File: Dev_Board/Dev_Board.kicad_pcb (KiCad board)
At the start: 2 copper layers, 41 x 67.7 mm, 31 parts, among them J1 Conn_01x04, J2 Conn_01x04

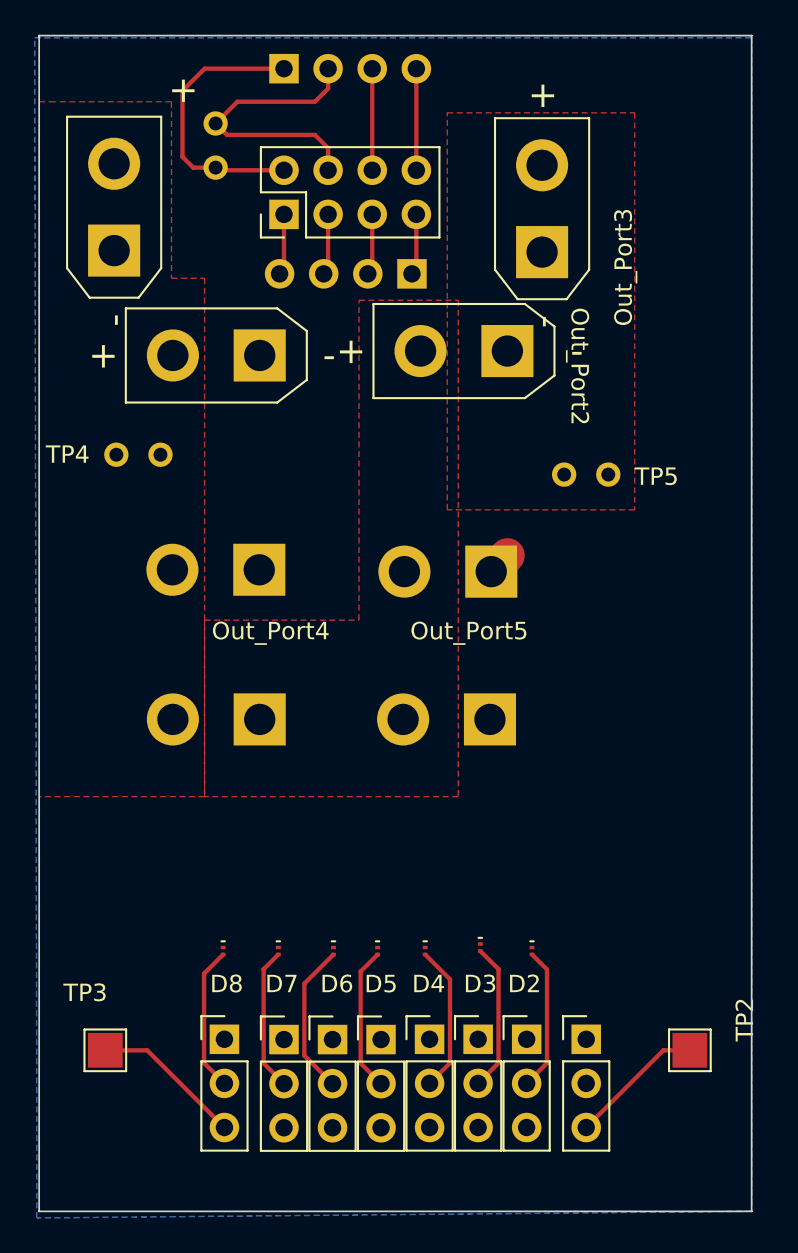
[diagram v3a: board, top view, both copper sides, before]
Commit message: Changed location of connectors of I2C and added mounting holes. Also I'm currently adding pads for the diodes
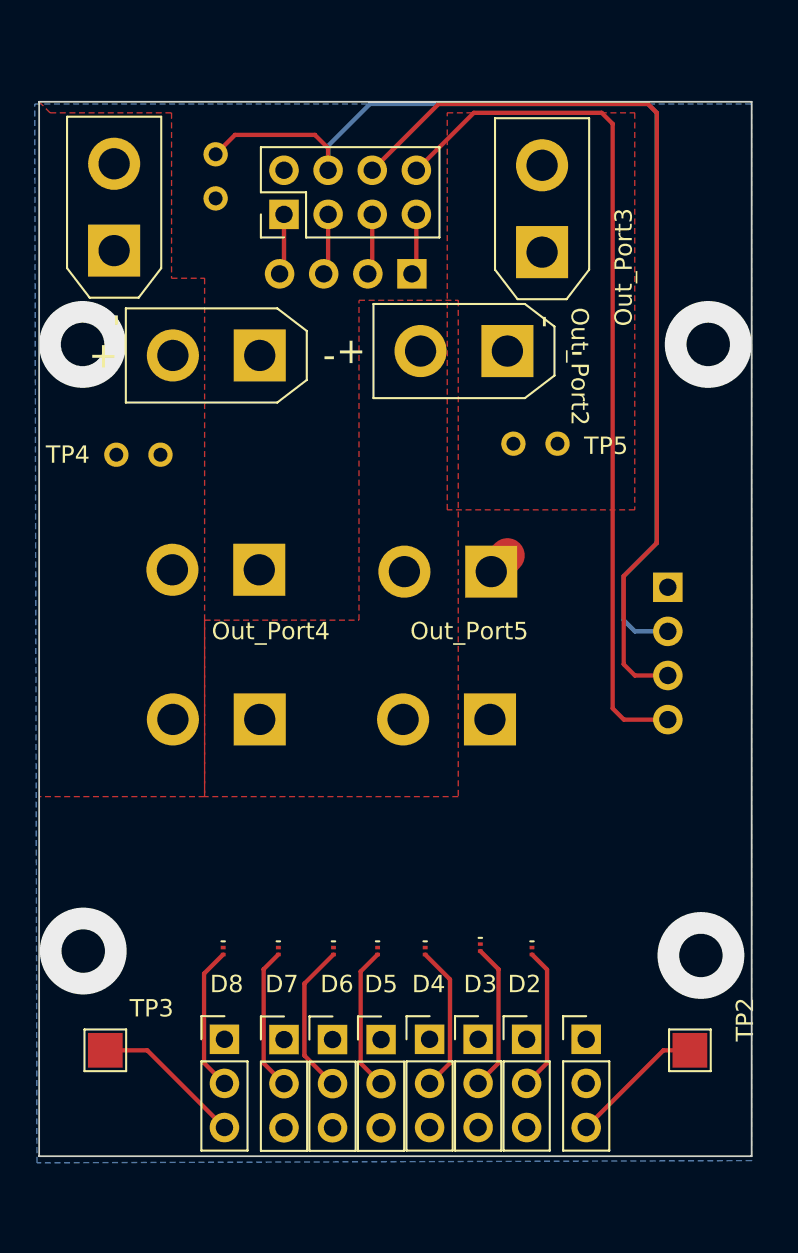
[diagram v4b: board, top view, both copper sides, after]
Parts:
- moved J2 37.1 mm to (222.2, 61.6), turned to 180 degrees
- moved TP5 3.42 mm to (213.4, 53.3)
- moved TP1 1.77 mm to (196.2, 39.2)
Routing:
- net /I2C2_SCL: track 5.85 -> 53.5 mm
- net +3.3V: track 16.8 -> 62.9 mm
- net /I2C2_SDA: track 5.85 -> 50.0 mm
- net GND: track 19.2 -> 3.06 mm, vias 0 -> 4
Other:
- board size 41 x 67.7 mm -> 41 x 60.7 mm

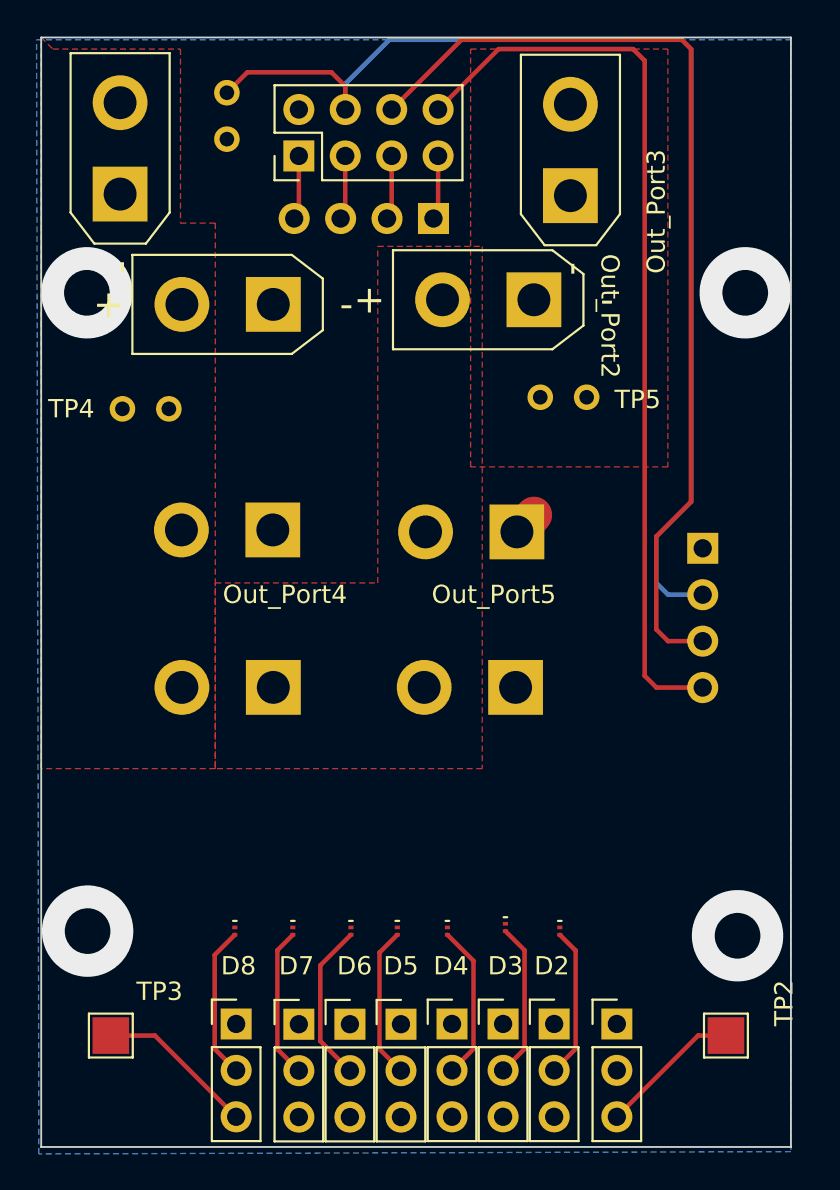
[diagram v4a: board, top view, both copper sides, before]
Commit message: fixed more sizing issues and I added a 1x4 connector to the data pins
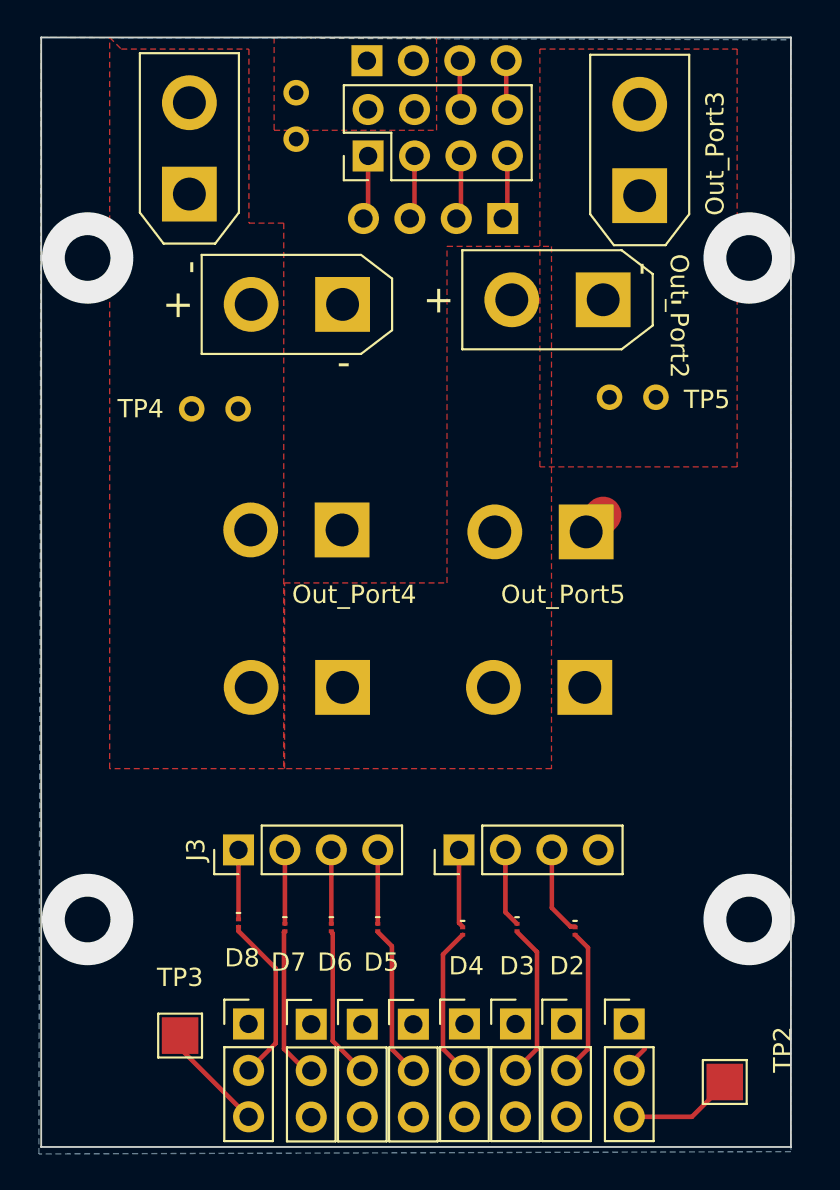
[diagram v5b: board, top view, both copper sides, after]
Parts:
- added J3: Conn_01x04, Connector_PinHeader_2.54mm:PinHeader_1x04_P2.54mm_Vertical, F.Cu at (196.8, 78.1)
- added J4: Conn_01x04, Connector_PinHeader_2.54mm:PinHeader_1x04_P2.54mm_Vertical, F.Cu at (208.9, 78.1)
- moved J2 32.4 mm to (203.9, 34.9), turned to -90 degrees
- moved IO_Port1 3.79 mm to (203.9, 40.1)
- moved In_Port1 3.79 mm to (194.2, 42.1)
- moved Out_Port4 3.79 mm to (202.4, 60.6)
- moved TP4 3.79 mm to (196.8, 54.0)
- moved In_Port2 3.79 mm to (202.4, 69.2)
- moved J1 3.79 mm to (211.3, 43.6)
- moved Out_Port1 3.79 mm to (202.4, 48.3)
- moved Out_Port2 3.79 mm to (216.7, 48.0)
- moved Out_Port3 3.79 mm to (218.8, 42.2)
- moved Out_Port5 3.79 mm to (215.8, 60.7)
- moved Out_Port6 3.79 mm to (215.7, 69.2)
- moved TP1 3.79 mm to (200.0, 39.2)
- moved TP3 3.79 mm to (193.7, 88.3)
- moved TP5 3.79 mm to (217.2, 53.3)
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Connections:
- D2 pad 1: unconnected-(D2-K-Pad1) -> Net-(D2-K)
- D3 pad 1: unconnected-(D3-K-Pad1) -> Net-(D3-K)
- D4 pad 1: unconnected-(D4-K-Pad1) -> Net-(D4-K)
- D5 pad 1: unconnected-(D5-K-Pad1) -> Net-(D5-K)
- D6 pad 1: unconnected-(D6-K-Pad1) -> Net-(D6-K)
- D7 pad 1: unconnected-(D7-K-Pad1) -> Net-(D7-K)
- D8 pad 1: unconnected-(D8-K-Pad1) -> Net-(D8-K)
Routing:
- net +3.3V: track 62.9 -> 0.00 mm
- net /I2C2_SCL: track 53.5 -> 2.70 mm
- net /I2C2_SDA: track 50.0 -> 2.70 mm
- net Net-(D2-K): track 0.00 -> 4.87 mm
- net Net-(D3-K): track 0.00 -> 4.31 mm
- net Net-(D4-K): track 0.00 -> 4.28 mm
- net Net-(D7-K): track 0.00 -> 4.05 mm
- net Net-(D6-K): track 0.00 -> 4.05 mm
- net Net-(D5-K): track 0.00 -> 4.05 mm
- net Net-(D8-K): track 0.00 -> 3.76 mm
- net /C8: track 8.70 -> 6.00 mm
- net /C1: track 7.81 -> 6.12 mm
- net /B1 (5V): track 0.00 -> 1.66 mm
- net /B8 (5V): track 8.36 -> 9.31 mm
- net /B6: track 8.80 -> 8.29 mm
- added copper zone on F.Cu, net +3.3V

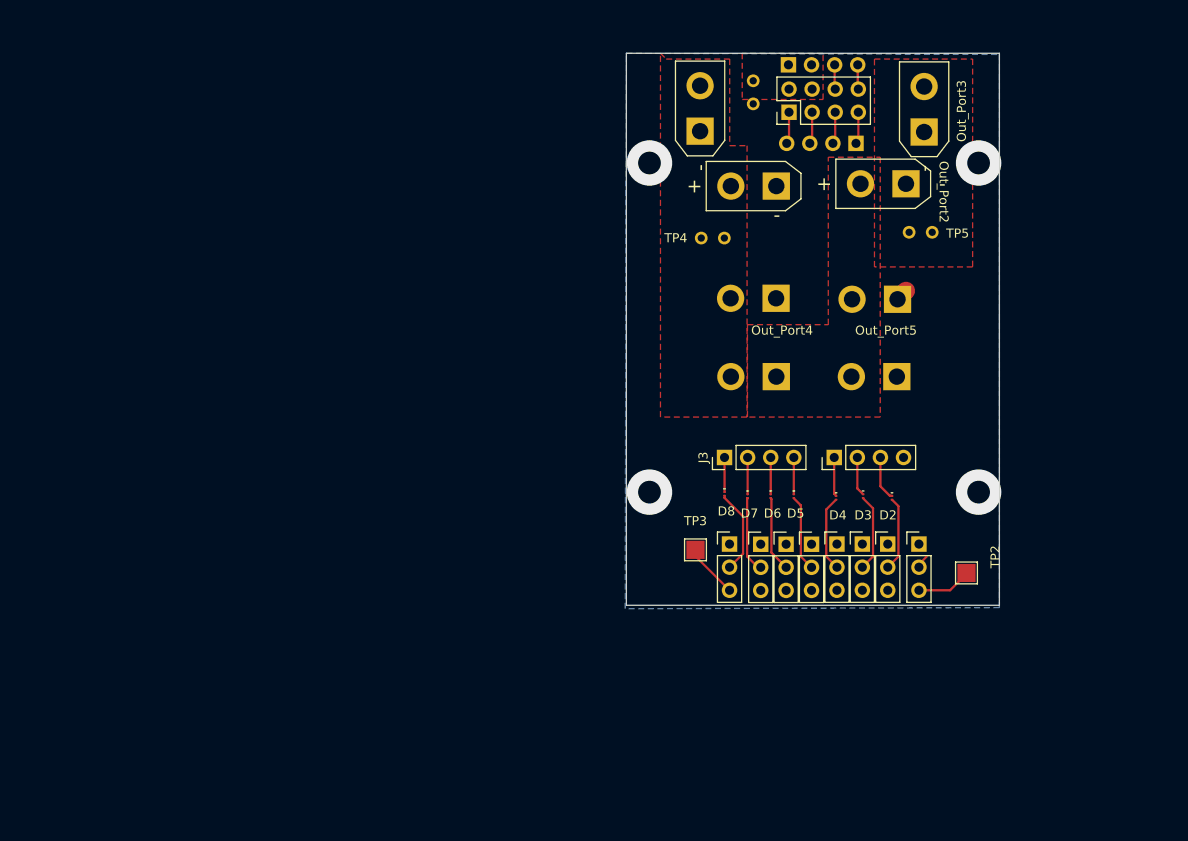
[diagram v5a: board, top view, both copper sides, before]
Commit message: Hopefully Final DevBoard. I flipped the data connectors and fixed label placement
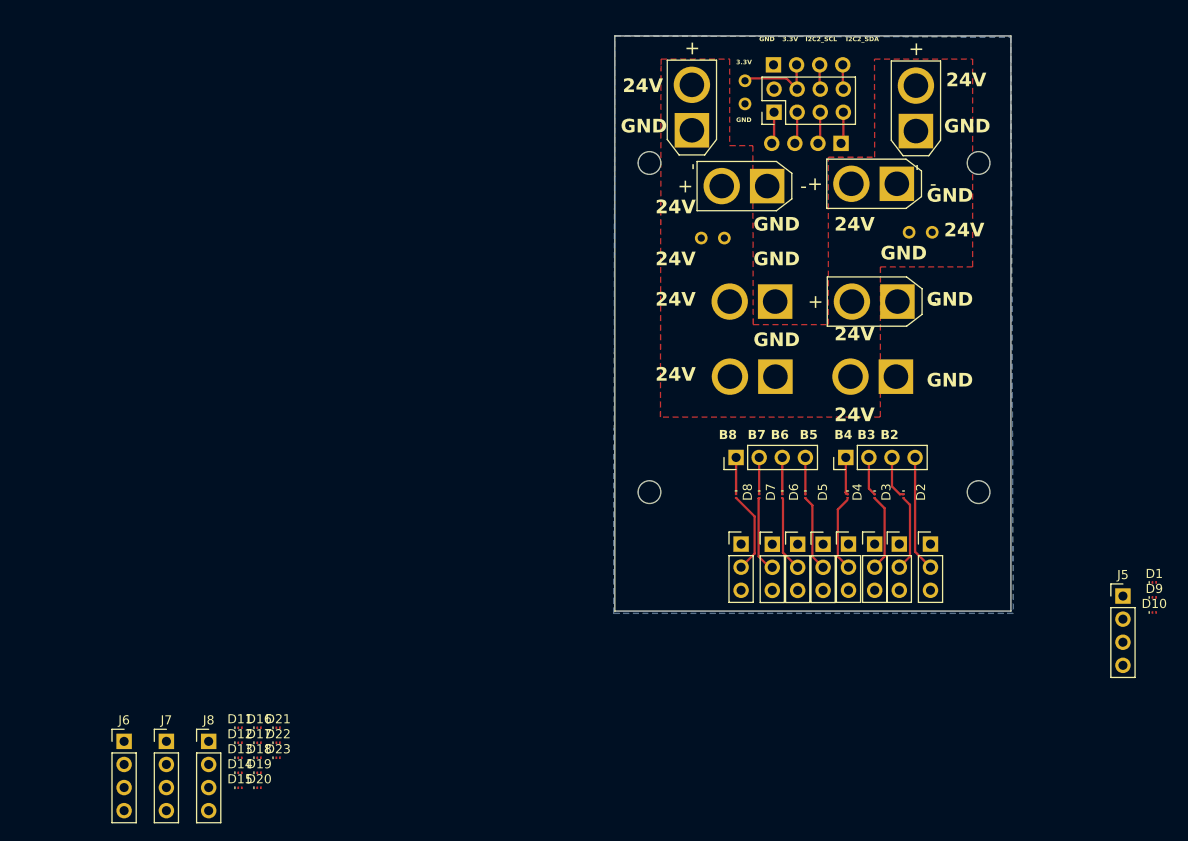
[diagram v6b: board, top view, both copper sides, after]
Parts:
- removed Out_Port5: Conn_01x02, dev_board_footprints:AMASS_XT30UPB-F_1x02_P5.0mm_Vertical_small_courtyards
- removed TP2, TP3: TestPoint, TestPoint:TestPoint_Pad_2.0x2.0mm
- added D1: D, Diode_SMD:Nexperia_DSN0603-2_0.6x0.3mm_P0.4mm, F.Cu at (244.1, 91.8)
- added D10: D, Diode_SMD:Nexperia_DSN0603-2_0.6x0.3mm_P0.4mm, F.Cu at (244.1, 95.1)
- added D11: D, Diode_SMD:Nexperia_DSN0603-2_0.6x0.3mm_P0.4mm, F.Cu at (143.6, 107.8)
- added D12: D, Diode_SMD:Nexperia_DSN0603-2_0.6x0.3mm_P0.4mm, F.Cu at (143.6, 109.5)
- added D13: D, Diode_SMD:Nexperia_DSN0603-2_0.6x0.3mm_P0.4mm, F.Cu at (143.6, 111.1)
- added D14: D, Diode_SMD:Nexperia_DSN0603-2_0.6x0.3mm_P0.4mm, F.Cu at (143.6, 112.8)
- added D15: D, Diode_SMD:Nexperia_DSN0603-2_0.6x0.3mm_P0.4mm, F.Cu at (143.6, 114.4)
- added D16: D, Diode_SMD:Nexperia_DSN0603-2_0.6x0.3mm_P0.4mm, F.Cu at (145.7, 107.8)
- added D17: D, Diode_SMD:Nexperia_DSN0603-2_0.6x0.3mm_P0.4mm, F.Cu at (145.7, 109.5)
- added D18: D, Diode_SMD:Nexperia_DSN0603-2_0.6x0.3mm_P0.4mm, F.Cu at (145.7, 111.1)
- added D19: D, Diode_SMD:Nexperia_DSN0603-2_0.6x0.3mm_P0.4mm, F.Cu at (145.7, 112.8)
- added D20: D, Diode_SMD:Nexperia_DSN0603-2_0.6x0.3mm_P0.4mm, F.Cu at (145.7, 114.4)
- added D21: D, Diode_SMD:Nexperia_DSN0603-2_0.6x0.3mm_P0.4mm, F.Cu at (147.8, 107.8)
- added D22: D, Diode_SMD:Nexperia_DSN0603-2_0.6x0.3mm_P0.4mm, F.Cu at (147.8, 109.5)
- added D23: D, Diode_SMD:Nexperia_DSN0603-2_0.6x0.3mm_P0.4mm, F.Cu at (147.8, 111.1)
- added D9: D, Diode_SMD:Nexperia_DSN0603-2_0.6x0.3mm_P0.4mm, F.Cu at (244.1, 93.5)
- added J5: Conn_01x04, Connector_PinHeader_2.54mm:PinHeader_1x04_P2.54mm_Vertical, F.Cu at (240.7, 93.3)
- added J6: Conn_01x04, Connector_PinHeader_2.54mm:PinHeader_1x04_P2.54mm_Vertical, F.Cu at (130.8, 109.3)
- added J7: Conn_01x04, Connector_PinHeader_2.54mm:PinHeader_1x04_P2.54mm_Vertical, F.Cu at (135.5, 109.3)
- added J8: Conn_01x04, Connector_PinHeader_2.54mm:PinHeader_1x04_P2.54mm_Vertical, F.Cu at (140.1, 109.3)
- added Out_Port8: Conn_01x02, Connector_AMASS:AMASS_XT30U-F_1x02_P5.0mm_Vertical, F.Cu at (215.9, 61.0)
- added REF**: MountingHole_2.5mm, MountingHole:MountingHole_2.5mm, F.Cu at (224.8, 81.9)
- added REF**: MountingHole_2.5mm, MountingHole:MountingHole_2.5mm, F.Cu at (188.6, 45.7)
- added REF**: MountingHole_2.5mm, MountingHole:MountingHole_2.5mm, F.Cu at (188.6, 81.9)
- added REF**: MountingHole_2.5mm, MountingHole:MountingHole_2.5mm, F.Cu at (224.8, 45.7)
- DBUS1, PWM_R1, PWM_R2, PWM_R3, PWM_R4, PWM_R5, PWM_R6, PWM_R7: footprint dev_board_footprints:PinHeader_1x03_2.54mm_Vertical_small_courtyards -> Connector_PinHeader_2.54mm:PinHeader_1x03_P2.54mm_Vertical
- In_Port1, In_Port2: footprint dev_board_footprints:AMASS_XT30UPB-M_1x02_P5.0mm_Vertical_small_courtyards -> Connector_AMASS:AMASS_XT30U-F_1x02_P5.0mm_Vertical
- Out_Port1, Out_Port2, Out_Port3, Out_Port4, Out_Port6: footprint dev_board_footprints:AMASS_XT30UPB-F_1x02_P5.0mm_Vertical_small_courtyards -> Connector_AMASS:AMASS_XT30U-F_1x02_P5.0mm_Vertical
- moved IO_Port1 1.65 mm to (202.3, 40.1)
- moved J2 1.65 mm to (202.2, 34.9)
- moved J1 1.64 mm to (209.7, 43.6)
- moved PWM_R3 1.35 mm to (213.4, 87.6)
- moved D8 1.29 mm to (198.1, 82.3)
- moved D2 1.29 mm to (216.5, 82.3)
- moved D4 1.29 mm to (210.4, 82.3)
- moved D3 1.27 mm to (213.4, 82.3)
- moved D5 1.27 mm to (205.7, 82.3)
- moved D7 1.27 mm to (200.7, 82.3)
- moved DBUS1 1.27 mm to (198.7, 87.6)
- moved J3 1.27 mm to (198.1, 78.1)
- moved J4 1.27 mm to (210.2, 78.1)
- moved PWM_R1 1.27 mm to (219.5, 87.6)
- moved PWM_R2 1.27 mm to (216.1, 87.6)
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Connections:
- net /B7 renamed Net-(D7-A)
- net /B8 (5V) renamed Net-(D8-A)
- D8 pad 1: Net-(D8-K) -> Net-(D21-A)
- DBUS1 pad 1: /A8M (GND) -> Net-(D15-A)
- J3 pad 1: Net-(D8-K) -> Net-(D21-A)
- J4 pad 4: unconnected-(J4-Pin_4-Pad4) -> /B1 (5V)
- PWM_R7 pad 1: /A7 -> Net-(D14-A)
- PWM_R7 pad 3: /C7 -> Net-(D21-A)
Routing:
- net /B1 (5V): track 1.66 -> 12.8 mm
- net +3.3V: track 0.00 -> 9.03 mm
- net /C1: track 6.12 -> 0.00 mm
- net /C8: track 6.00 -> 0.00 mm
- net Net-(D21-A): track 0.00 -> 3.99 mm
- net Net-(D8-K): track 3.76 -> 0.00 mm
- net GND: track 3.06 -> 1.75 mm, vias 4 -> 0
- removed copper zone on F.Cu, net +3.3V
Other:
- board size 41 x 60.7 mm -> 43.6 x 63.2 mm
- board text added: "24V"
- board text added: "3.3V"
- board text added: "B2"
- board text added: "B3"
- board text added: "B4"
- board text added: "B5"
- board text added: "B6"
- board text added: "B7"
- board text added: "B8"
- board text added: "GND"
- board text added: "I2C2_SCL"
- board text added: "I2C2_SDA"
